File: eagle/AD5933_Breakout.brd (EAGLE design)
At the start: 38.1 x 25.4 mm, 6 parts, among them U1 AD5933

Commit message: both board and schematic looking good
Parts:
- removed JP3: (no value), SparkFun-Connectors:1X04
- added JP1: (no value), SparkFun-Connectors:1X04
- moved JP2 22.9 mm to (15.2, 24.1)
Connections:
- removed net DVDD: C1.1, C2.1, U1.10, U1.11, U1.9
- new net MCLK: JP1.3, U1.8
- new net SCL: JP1.1, U1.16
- new net SDA: JP1.2, U1.15
- new net VCC: C1.1, C2.1, JP2.1, U1.10, U1.11, U1.9
- net GND: now also JP1.4
- net RFB: now also JP2.3
- net VIN: now also JP2.2
- net VOUT: now also JP2.4
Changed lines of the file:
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@@
 <attribute name="PROD_ID" value="CAP-08390" x="31.75" y="54.61" size="1.778" layer="27" rot="R90" display="off"/>
 </element>
-<element name="JP2" library="SparkFun-Connectors" package="1X04" value="" x="15.24" y="1.27"/>
-<element name="JP3" library="SparkFun-Connectors" package="1X04" value="" x="15.24" y="24.13"/>
+<element name="JP1" library="SparkFun-Connectors" package="1X04" value="" x="15.24" y="1.27"/>
+<element name="JP2" library="SparkFun-Connectors" package="1X04" value="" x="15.24" y="24.13"/>
 </elements>
 <signals>
 <signal name="VIN">
 <contactref element="U1" pad="5"/>
+<contactref element="JP2" pad="2"/>
+<wire x1="19.37" y1="9" x2="17.78" y2="24.13" width="0" layer="19" extent="1-1"/>
 </signal>
 <signal name="RFB">
 <contactref element="U1" pad="4"/>
+<contactref element="JP2" pad="3"/>
+<wire x1="18.73" y1="9" x2="20.32" y2="24.13" width="0" layer="19" extent="1-1"/>
 </signal>
 <signal name="VOUT">
 <contactref element="U1" pad="6"/>
+<contactref element="JP2" pad="4"/>
+<wire x1="20.01" y1="9" x2="22.86" y2="24.13" width="0" layer="19" extent="1-1"/>
 </signal>
 <signal name="GND">
@@
 <contactref element="U1" pad="13"/>
 <contactref element="U1" pad="14"/>
-<wire x1="18.73" y1="16.4" x2="19.37" y2="16.4" width="0" layer="19" extent="1-1"/>
-<wire x1="18.09" y1="16.4" x2="18.73" y2="16.4" width="0" layer="19" extent="1-1"/>
-<wire x1="13.97" y1="13.55" x2="18.09" y2="16.4" width="0" layer="19" extent="1-1"/>
-<wire x1="10.16" y1="13.55" x2="13.97" y2="13.55" width="0" layer="19" extent="1-1"/>
+<contactref element="JP1" pad="4"/>
+<wire x1="10.16" y1="13.55" x2="22.86" y2="1.27" width="0" layer="19" extent="1-1"/>
+<wire x1="13.97" y1="13.55" x2="10.16" y2="13.55" width="0" layer="19" extent="1-1"/>
+<wire x1="18.09" y1="16.4" x2="13.97" y2="13.55" width="0" layer="19" extent="1-1"/>
+<wire x1="18.73" y1="16.4" x2="18.09" y2="16.4" width="0" layer="19" extent="1-1"/>
+<wire x1="19.37" y1="16.4" x2="18.73" y2="16.4" width="0" layer="19" extent="1-1"/>
 </signal>
-<signal name="DVDD">
+<signal name="SCL">
+<contactref element="JP1" pad="1"/>
+<contactref element="U1" pad="16"/>
+<wire x1="15.24" y1="1.27" x2="16.81" y2="16.4" width="0" layer="19" extent="1-1"/>
+</signal>
+<signal name="SDA">
+<contactref element="JP1" pad="2"/>
+<contactref element="U1" pad="15"/>
+<wire x1="17.78" y1="1.27" x2="17.45" y2="16.4" width="0" layer="19" extent="1-1"/>
+</signal>
+<signal name="MCLK">
+<contactref element="JP1" pad="3"/>
+<contactref element="U1" pad="8"/>
+<wire x1="20.32" y1="1.27" x2="21.29" y2="9" width="0" layer="19" extent="1-1"/>
+</signal>
+<signal name="VCC">
+<contactref element="JP2" pad="1"/>
 <contactref element="U1" pad="9"/>
 <contactref element="U1" pad="11"/>
@@
 <contactref element="C1" pad="1"/>
 <contactref element="C2" pad="1"/>
-<wire x1="20.65" y1="16.4" x2="21.29" y2="16.4" width="0" layer="19" extent="1-1"/>
-<wire x1="20.01" y1="16.4" x2="20.65" y2="16.4" width="0" layer="19" extent="1-1"/>
+<wire x1="20.01" y1="16.4" x2="15.24" y2="24.13" width="0" layer="19" extent="1-1"/>
+<wire x1="20.65" y1="16.4" x2="20.01" y2="16.4" width="0" layer="19" extent="1-1"/>
+<wire x1="21.29" y1="16.4" x2="20.65" y2="16.4" width="0" layer="19" extent="1-1"/>
 <wire x1="13.97" y1="11.85" x2="20.01" y2="16.4" width="0" layer="19" extent="1-1"/>
 <wire x1="10.16" y1="11.85" x2="13.97" y2="11.85" width="0" layer="19" extent="1-1"/>

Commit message: first pcb routing
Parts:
- moved JP1 1.27 mm to (15.2, 2.54)
- moved JP2 1.27 mm to (15.2, 22.9)
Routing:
- net GND: track 0.00 -> 40.3 mm, vias 0 -> 1
- net VCC: track 0.00 -> 28.0 mm
- net SDA: track 0.00 -> 17.2 mm
- net VIN: track 0.00 -> 17.1 mm, vias 0 -> 1
- net RFB: track 0.00 -> 14.9 mm, vias 0 -> 1
- net SCL: track 0.00 -> 14.5 mm
- net MCLK: track 0.00 -> 9.13 mm
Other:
- board size 38.1 x 25.4 mm -> 36.8 x 25.4 mm

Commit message: rerouted board
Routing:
- net GND: track 40.3 -> 45.5 mm, vias 1 -> 0
- net VCC: track 28.0 -> 24.1 mm
- net MCLK: track 9.13 -> 6.90 mm
- net VIN: track 17.1 -> 14.9 mm
- net SDA: track 17.2 -> 15.0 mm
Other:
- board size 36.8 x 25.4 mm -> 38.1 x 25.4 mm
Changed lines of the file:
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@@
 <board>
 <plain>
-<wire x1="0" y1="0" x2="36.83" y2="0" width="0" layer="20"/>
-<wire x1="36.83" y1="0" x2="36.83" y2="25.4" width="0" layer="20"/>
-<wire x1="36.83" y1="25.4" x2="0" y2="25.4" width="0" layer="20"/>
+<wire x1="0" y1="0" x2="38.1" y2="0" width="0" layer="20"/>
+<wire x1="38.1" y1="0" x2="38.1" y2="25.4" width="0" layer="20"/>
+<wire x1="38.1" y1="25.4" x2="0" y2="25.4" width="0" layer="20"/>
 <wire x1="0" y1="25.4" x2="0" y2="0" width="0" layer="20"/>
 <text x="15.24" y="5.08" size="0.8128" layer="21" font="vector" ratio="15" rot="R90">SCL</text>
@@
 <contactref element="JP2" pad="2"/>
 <wire x1="19.304" y1="13.6144" x2="19.304" y2="9.144" width="0.254" layer="1"/>
-<wire x1="19.304" y1="23.1648" x2="19.304" y2="13.6144" width="0.254" layer="16"/>
-<wire x1="18.6944" y1="23.1648" x2="19.304" y2="23.1648" width="0.254" layer="16"/>
-<wire x1="17.8816" y1="23.9776" x2="18.6944" y2="23.1648" width="0.254" layer="16"/>
+<wire x1="19.304" y1="21.9456" x2="19.304" y2="13.6144" width="0.254" layer="16"/>
+<wire x1="18.6944" y1="21.9456" x2="19.304" y2="21.9456" width="0.254" layer="16"/>
+<wire x1="17.78" y1="22.86" x2="18.6944" y2="21.9456" width="0.254" layer="16"/>
 <wire x1="19.304" y1="9.144" x2="19.37" y2="9" width="0.254" layer="1"/>
-<wire x1="17.8816" y1="23.9776" x2="17.78" y2="22.86" width="0.254" layer="16"/>
 <via x="19.304" y="13.6144" extent="1-16" drill="0.6096"/>
 </signal>
@@
 <contactref element="U1" pad="14"/>
 <contactref element="JP1" pad="4"/>
-<wire x1="13.8176" y1="13.6144" x2="12.5984" y2="13.6144" width="0.254" layer="1"/>
-<wire x1="12.5984" y1="13.6144" x2="10.16" y2="13.6144" width="0.254" layer="1"/>
+<wire x1="13.8176" y1="13.6144" x2="10.16" y2="13.6144" width="0.254" layer="1"/>
 <wire x1="10.16" y1="13.6144" x2="10.16" y2="13.55" width="0.254" layer="1"/>
 <wire x1="13.8176" y1="13.6144" x2="13.97" y2="13.55" width="0.254" layer="1"/>
@@
 <wire x1="19.304" y1="14.8336" x2="19.304" y2="16.256" width="0.254" layer="1"/>
 <wire x1="22.7584" y1="11.3792" x2="19.304" y2="14.8336" width="0.254" layer="1"/>
-<wire x1="22.7584" y1="1.4224" x2="22.7584" y2="11.3792" width="0.254" layer="1"/>
+<wire x1="22.7584" y1="2.6416" x2="22.7584" y2="11.3792" width="0.254" layer="1"/>
 <wire x1="19.304" y1="16.256" x2="19.37" y2="16.4" width="0.254" layer="1"/>
-<wire x1="22.7584" y1="1.4224" x2="22.86" y2="2.54" width="0.254" layer="1"/>
-<wire x1="12.5984" y1="13.0048" x2="12.5984" y2="13.6144" width="0.254" layer="1"/>
-<wire x1="22.7584" y1="2.8448" x2="12.5984" y2="13.0048" width="0.254" layer="16"/>
-<wire x1="22.7584" y1="1.4224" x2="22.7584" y2="2.8448" width="0.254" layer="16"/>
-<wire x1="22.7584" y1="1.4224" x2="22.86" y2="2.54" width="0.254" layer="16"/>
-<via x="12.5984" y="13.0048" extent="1-16" drill="0.6096"/>
+<wire x1="22.7584" y1="2.6416" x2="22.86" y2="2.54" width="0.254" layer="1"/>
+<wire x1="9.144" y1="12.3952" x2="10.16" y2="13.4112" width="0.254" layer="1"/>
+<wire x1="9.144" y1="6.096" x2="9.144" y2="12.3952" width="0.254" layer="1"/>
+<wire x1="14.0208" y1="1.2192" x2="9.144" y2="6.096" width="0.254" layer="1"/>
+<wire x1="22.7584" y1="1.2192" x2="14.0208" y2="1.2192" width="0.254" layer="1"/>
+<wire x1="22.7584" y1="2.4384" x2="22.7584" y2="1.2192" width="0.254" layer="1"/>
+<wire x1="10.16" y1="13.4112" x2="10.16" y2="13.55" width="0.254" layer="1"/>
+<wire x1="22.7584" y1="2.4384" x2="22.86" y2="2.54" width="0.254" layer="1"/>
 </signal>
 <signal name="SCL">
@@
 <wire x1="17.4752" y1="11.7856" x2="17.4752" y2="16.256" width="0.254" layer="1"/>
 <wire x1="16.256" y1="10.5664" x2="17.4752" y2="11.7856" width="0.254" layer="1"/>
-<wire x1="16.256" y1="2.8448" x2="16.256" y2="10.5664" width="0.254" layer="1"/>
-<wire x1="17.6784" y1="1.4224" x2="16.256" y2="2.8448" width="0.254" layer="1"/>
+<wire x1="16.256" y1="4.064" x2="16.256" y2="10.5664" width="0.254" layer="1"/>
+<wire x1="17.78" y1="2.54" x2="16.256" y2="4.064" width="0.254" layer="1"/>
 <wire x1="17.4752" y1="16.256" x2="17.45" y2="16.4" width="0.254" layer="1"/>
-<wire x1="17.6784" y1="1.4224" x2="17.78" y2="2.54" width="0.254" layer="1"/>
 </signal>
 <signal name="MCLK">
 <contactref element="JP1" pad="3"/>
 <contactref element="U1" pad="8"/>
-<wire x1="21.336" y1="2.4384" x2="21.336" y2="8.9408" width="0.254" layer="1"/>
-<wire x1="20.32" y1="1.4224" x2="21.336" y2="2.4384" width="0.254" layer="1"/>
+<wire x1="21.336" y1="3.6576" x2="21.336" y2="8.9408" width="0.254" layer="1"/>
+<wire x1="20.32" y1="2.6416" x2="21.336" y2="3.6576" width="0.254" layer="1"/>
 <wire x1="21.336" y1="8.9408" x2="21.29" y2="9" width="0.254" layer="1"/>
-<wire x1="20.32" y1="1.4224" x2="20.32" y2="2.54" width="0.254" layer="1"/>
+<wire x1="20.32" y1="2.6416" x2="20.32" y2="2.54" width="0.254" layer="1"/>
 </signal>
 <signal name="VCC">
@@
 <wire x1="21.1328" y1="16.4592" x2="21.29" y2="16.4" width="0.254" layer="1"/>
 <wire x1="20.7264" y1="16.4592" x2="20.65" y2="16.4" width="0.254" layer="1"/>
-<wire x1="20.1168" y1="19.1008" x2="20.1168" y2="16.4592" width="0.254" layer="1"/>
-<wire x1="15.24" y1="23.9776" x2="16.256" y2="22.9616" width="0.254" layer="1"/>
-<wire x1="16.256" y1="22.9616" x2="20.1168" y2="19.1008" width="0.254" layer="1"/>
+<wire x1="20.1168" y1="17.9832" x2="20.1168" y2="16.4592" width="0.254" layer="1"/>
+<wire x1="15.24" y1="22.7584" x2="16.256" y2="21.7424" width="0.254" layer="1"/>
 <wire x1="20.1168" y1="16.4592" x2="20.01" y2="16.4" width="0.254" layer="1"/>
-<wire x1="15.24" y1="23.9776" x2="15.24" y2="22.86" width="0.254" layer="1"/>
+<wire x1="15.24" y1="22.7584" x2="15.24" y2="22.86" width="0.254" layer="1"/>
 <wire x1="16.256" y1="14.224" x2="14.0208" y2="11.9888" width="0.254" layer="1"/>
-<wire x1="16.256" y1="22.9616" x2="16.256" y2="14.224" width="0.254" layer="1"/>
+<wire x1="16.256" y1="21.7424" x2="16.256" y2="20.32" width="0.254" layer="1"/>
+<wire x1="16.256" y1="20.32" x2="16.256" y2="14.224" width="0.254" layer="1"/>
 <wire x1="14.0208" y1="11.9888" x2="13.97" y2="11.85" width="0.254" layer="1"/>
+<wire x1="20.1168" y1="17.9832" x2="17.78" y2="20.32" width="0.254" layer="1"/>
+<wire x1="17.78" y1="20.32" x2="16.256" y2="20.32" width="0.254" layer="1"/>
 </signal>
 </signals>

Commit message: discovered downloaded ad5933 footprint is buggy
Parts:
- moved FRAME1 39.5 mm to (-10.2, -14.0)
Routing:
- net VCC: track 24.1 -> 24.6 mm
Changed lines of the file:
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@@
 </pass>
 <pass name="Follow-me" refer="Default" active="yes">
+<param name="mnVias" value="30"/>
 </pass>
 <pass name="Busses" refer="Default" active="yes">
@@
 <elements>
 <element name="U1" library="kblom" package="SSOP16" value="AD5933" x="19.05" y="12.7"/>
-<element name="FRAME1" library="SparkFun-Aesthetics" package="CREATIVE_COMMONS" value="FRAME-LETTER" x="11.43" y="-46.99"/>
+<element name="FRAME1" library="SparkFun-Aesthetics" package="CREATIVE_COMMONS" value="FRAME-LETTER" x="-10.16" y="-13.97"/>
 <element name="C1" library="SparkFun-Capacitors" package="0603-CAP" value="0.1uF" x="13.97" y="12.7" rot="R90">
 <attribute name="PROD_ID" value="CAP-08390" x="35.56" y="50.8" size="1.778" layer="27" rot="R90" display="off"/>
@@
 <wire x1="21.1328" y1="16.4592" x2="21.29" y2="16.4" width="0.254" layer="1"/>
 <wire x1="20.7264" y1="16.4592" x2="20.65" y2="16.4" width="0.254" layer="1"/>
-<wire x1="20.1168" y1="17.9832" x2="20.1168" y2="16.4592" width="0.254" layer="1"/>
+<wire x1="20.1168" y1="17.8816" x2="20.1168" y2="16.4592" width="0.254" layer="1"/>
 <wire x1="15.24" y1="22.7584" x2="16.256" y2="21.7424" width="0.254" layer="1"/>
+<wire x1="16.256" y1="21.7424" x2="20.1168" y2="17.8816" width="0.254" layer="1"/>
 <wire x1="20.1168" y1="16.4592" x2="20.01" y2="16.4" width="0.254" layer="1"/>
 <wire x1="15.24" y1="22.7584" x2="15.24" y2="22.86" width="0.254" layer="1"/>
 <wire x1="16.256" y1="14.224" x2="14.0208" y2="11.9888" width="0.254" layer="1"/>
-<wire x1="16.256" y1="21.7424" x2="16.256" y2="20.32" width="0.254" layer="1"/>
-<wire x1="16.256" y1="20.32" x2="16.256" y2="14.224" width="0.254" layer="1"/>
+<wire x1="16.256" y1="21.7424" x2="16.256" y2="14.224" width="0.254" layer="1"/>
 <wire x1="14.0208" y1="11.9888" x2="13.97" y2="11.85" width="0.254" layer="1"/>
-<wire x1="20.1168" y1="17.9832" x2="17.78" y2="20.32" width="0.254" layer="1"/>
-<wire x1="17.78" y1="20.32" x2="16.256" y2="20.32" width="0.254" layer="1"/>
 </signal>
 </signals>

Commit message: clean up
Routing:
- net VCC: track 24.6 -> 24.1 mm
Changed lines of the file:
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@@
 <wire x1="21.1328" y1="16.4592" x2="21.29" y2="16.4" width="0.254" layer="1"/>
 <wire x1="20.7264" y1="16.4592" x2="20.65" y2="16.4" width="0.254" layer="1"/>
-<wire x1="20.1168" y1="17.8816" x2="20.1168" y2="16.4592" width="0.254" layer="1"/>
+<wire x1="20.1168" y1="17.9832" x2="20.1168" y2="16.4592" width="0.254" layer="1"/>
 <wire x1="15.24" y1="22.7584" x2="16.256" y2="21.7424" width="0.254" layer="1"/>
-<wire x1="16.256" y1="21.7424" x2="20.1168" y2="17.8816" width="0.254" layer="1"/>
 <wire x1="20.1168" y1="16.4592" x2="20.01" y2="16.4" width="0.254" layer="1"/>
 <wire x1="15.24" y1="22.7584" x2="15.24" y2="22.86" width="0.254" layer="1"/>
 <wire x1="16.256" y1="14.224" x2="14.0208" y2="11.9888" width="0.254" layer="1"/>
-<wire x1="16.256" y1="21.7424" x2="16.256" y2="14.224" width="0.254" layer="1"/>
+<wire x1="16.256" y1="21.7424" x2="16.256" y2="20.32" width="0.254" layer="1"/>
+<wire x1="16.256" y1="20.32" x2="16.256" y2="14.224" width="0.254" layer="1"/>
 <wire x1="14.0208" y1="11.9888" x2="13.97" y2="11.85" width="0.254" layer="1"/>
+<wire x1="20.1168" y1="17.9832" x2="17.78" y2="20.32" width="0.254" layer="1"/>
+<wire x1="17.78" y1="20.32" x2="16.256" y2="20.32" width="0.254" layer="1"/>
 </signal>
 </signals>

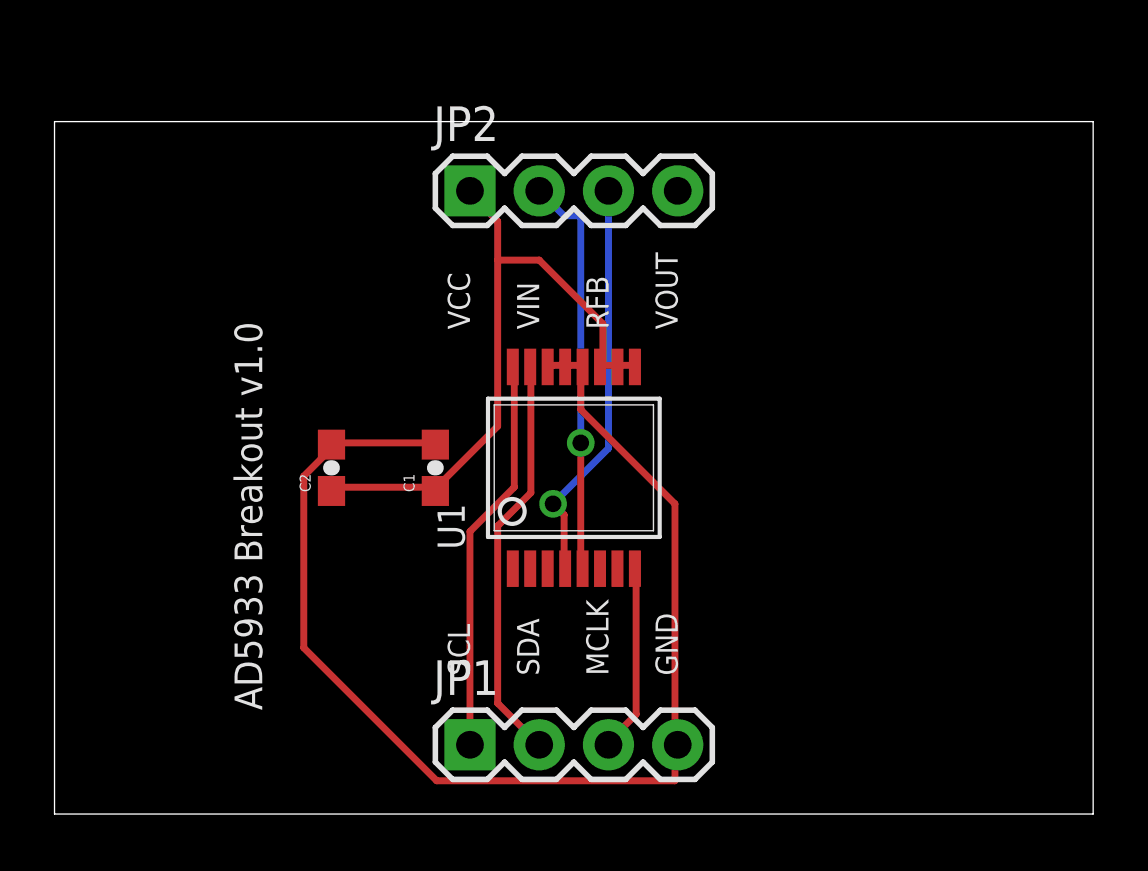
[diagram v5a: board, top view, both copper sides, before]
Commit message: switched headers and rerouted all pins
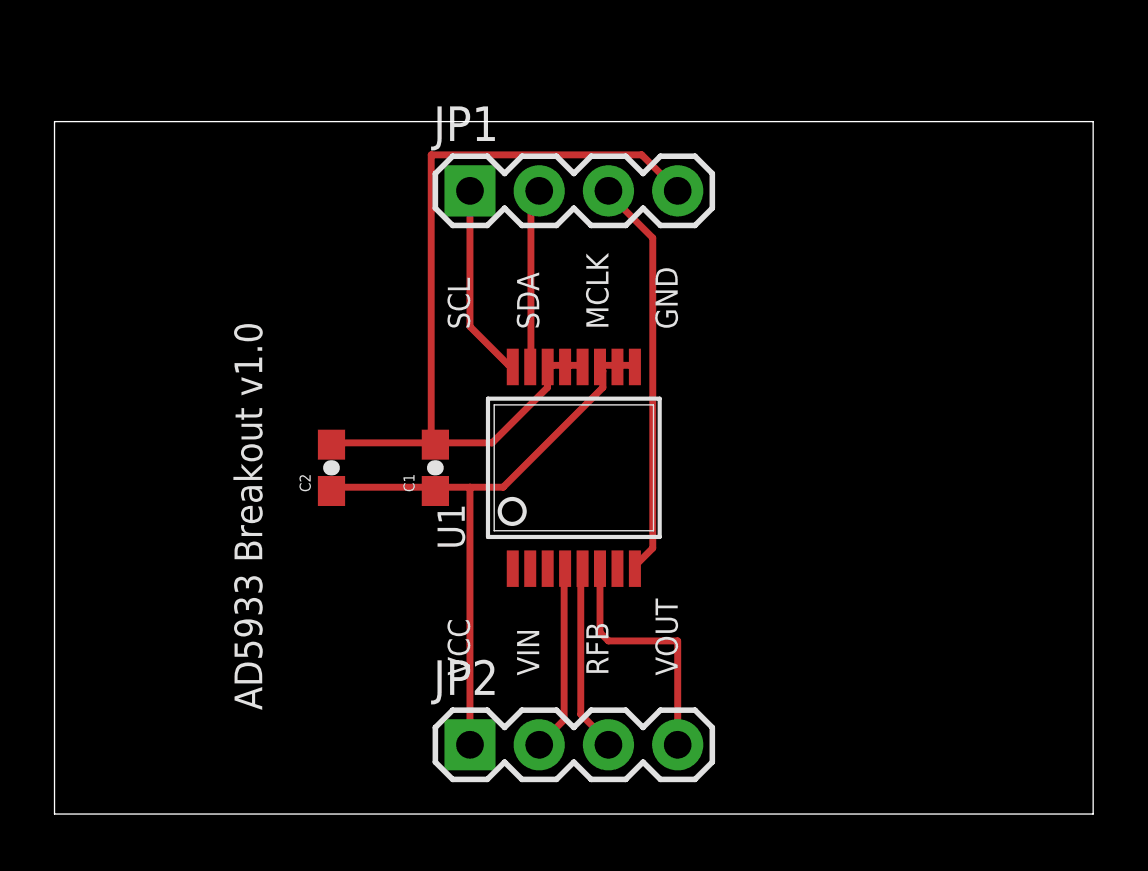
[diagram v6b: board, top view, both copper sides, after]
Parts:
- moved JP1 20.3 mm to (15.2, 22.9)
- moved JP2 20.3 mm to (15.2, 2.54)
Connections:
- net RFB: now also JP2.2; no longer JP2.3
- net VIN: now also JP2.3; no longer JP2.2
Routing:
- net GND: track 45.5 -> 31.1 mm
- net VOUT: track 0.00 -> 9.13 mm
- net SDA: track 15.0 -> 6.59 mm
- net RFB: track 14.9 -> 6.85 mm, vias 1 -> 0
- net VIN: track 14.9 -> 6.91 mm, vias 1 -> 0
- net MCLK: track 6.90 -> 14.8 mm
- net SCL: track 14.5 -> 7.15 mm
- net VCC: track 24.1 -> 23.3 mm
